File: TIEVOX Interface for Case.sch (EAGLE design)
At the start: 22 parts, among them U4 CAT24C32.UDFN8

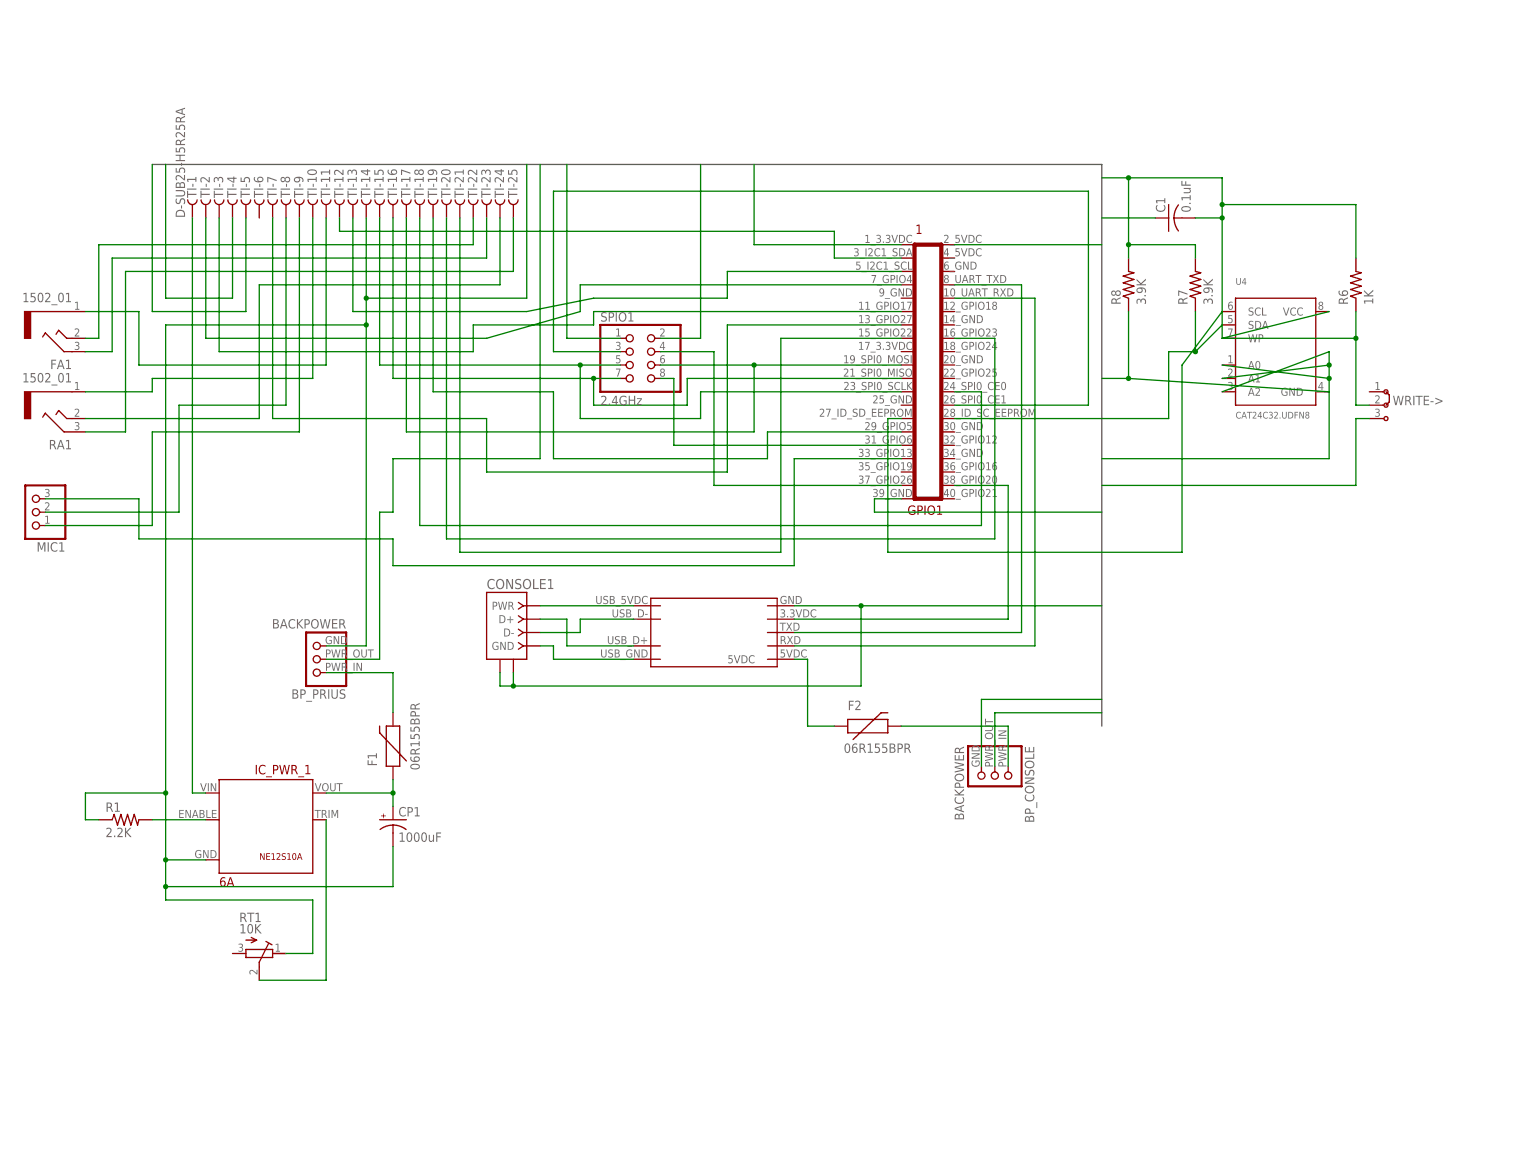
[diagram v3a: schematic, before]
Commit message: Updated TIEVOX Interface for Case:
- Removed console circuit
- Replaced audio jacks to use ones purchased
- Remapped circuit schematic
- Added backpower protection back in
- Still needs traces drawn.
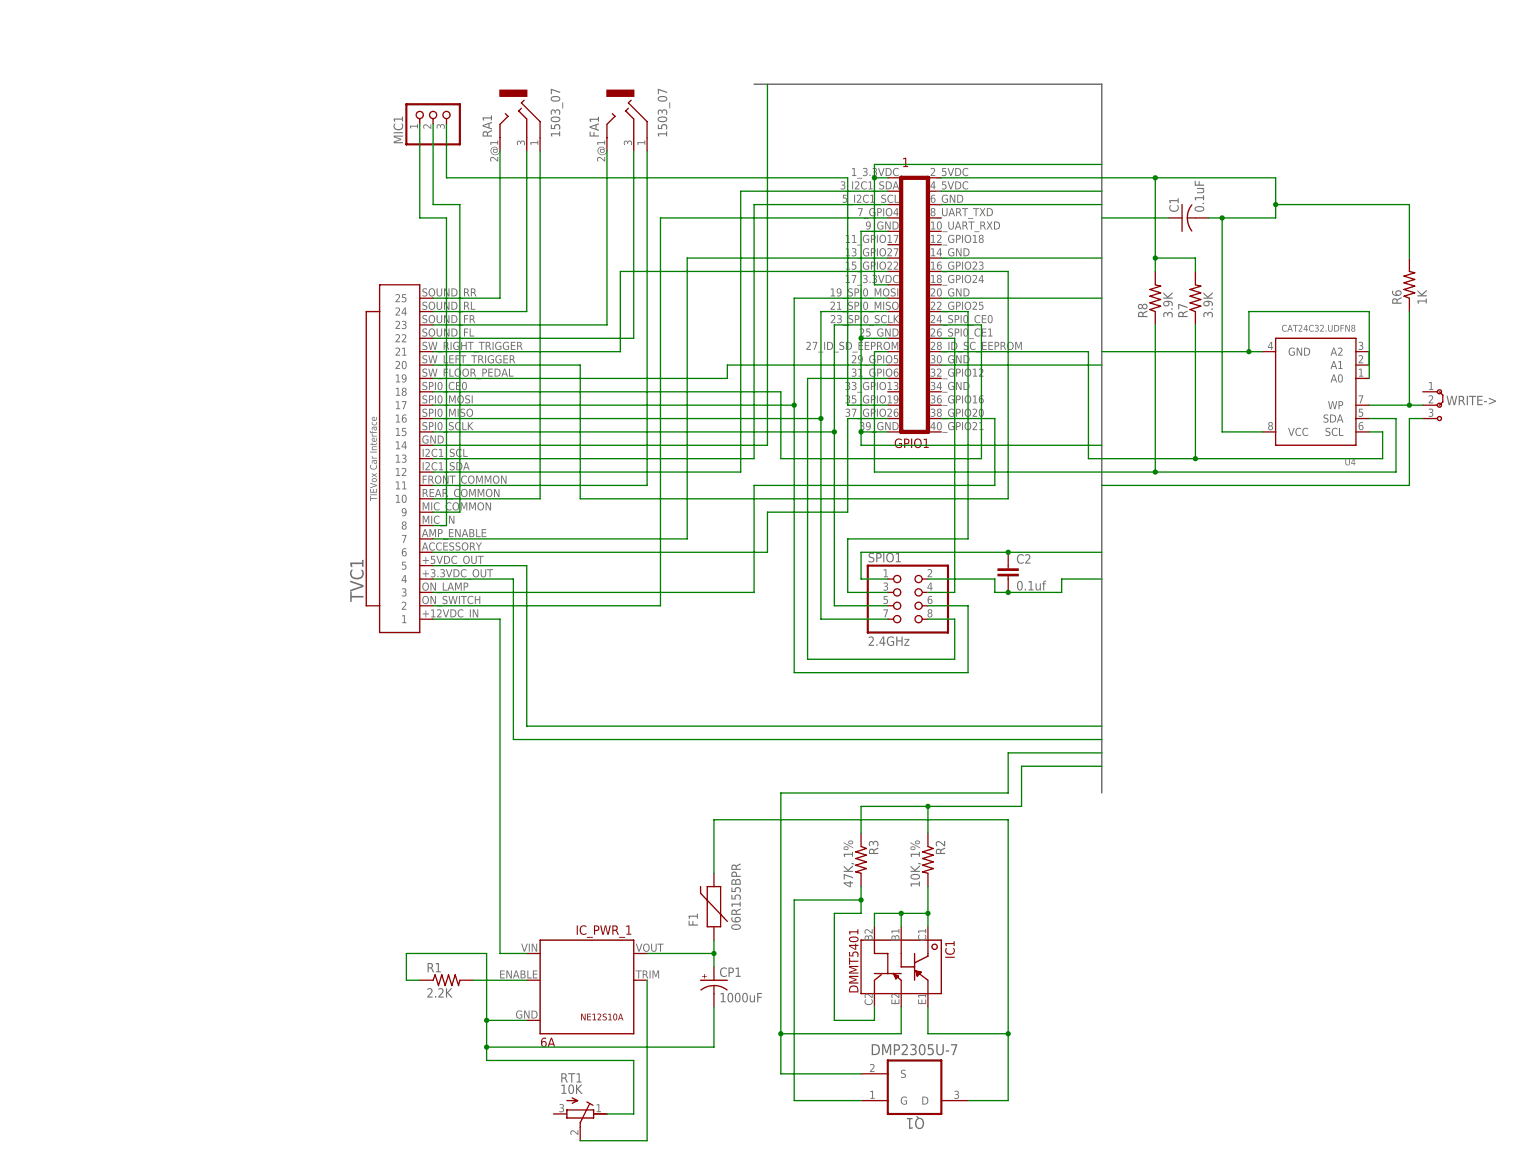
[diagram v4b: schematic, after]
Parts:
- removed BP_CONSOLE, BP_PRIUS: BACKPOWER, connectors:BACKPOWER
- removed CONSOLE1: (no value), connector:USB-RA
- removed F2: 06R155BPR, SparkFun-PowerIC:PTCPTH
- removed TI: D-SUB25-H5R25RA, con-thomas-betts:D-SUB25-H5R25RA
- removed UART1: GS27159, packages:GS27159
- added C2: 0.1uf, capacitor-wima:C5/2.5
- added IC1: DMMT5401, Diodes_Inc_By_element14_Batch_1:DMMT5401DMMT
- added Q1: DMP2305U-7, Diodes_Inc_By_element14_Batch_1:DMP2305U-7
- added R2: 10K, 1%, adafruit:R-US_0207/7
- added R3: 47K, 1%, adafruit:R-US_0207/7
- added TVC1: TIEVox Car Interface, connectors:TIEVOX_CAR_25
- FA1, RA1: value 1502_01 -> 1503_07; device con-lumberg:1502_01 -> con-lumberg:1503_07
- GPIO1: value RPI_GPIO_FEMALE_LOWER -> RPI_GPIO_MALE_SHROUD; device connectors:RPI_GPIO_FEMALE_LOWER -> connectors:RPI_GPIO_MALE_SHROUD
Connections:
- removed net 5VDC: F2.1, UART1.5VDC
- removed net CONSOLE_ON: GPIO1.38_GPIO20, UART1.3.3VDC
- removed net N$11 (its old number): GPIO1.29_GPIO5, TI-19.F
- removed net N$31: BP_CONSOLE.PWR_IN, F2.2
- removed net N$36: MIC1.1, TI-9.F
- removed net N$37: MIC1.2, TI-8.F
- removed net N$38: GPIO1.27_ID_SC_EEPROM, U4.SCL
- removed net N$40: GPIO1.28_ID_SC_EEPROM, R7.1, U4.SDA
- removed net N$41: GPIO1.33_GPIO13, MIC1.3
- new net IN: F1.2, IC1.E1, Q1.D
- new net N$32: IC1.B1, IC1.B2, IC1.C1, R2.2
- new net N$33: IC1.C2, Q1.G, R3.2
- new net N$5: FA1.1, TVC1.11
- net +3.3VDC: now also C2.2, GPIO1.17_3.3VDC, TVC1.4; no longer TI-4.F
- net +5VDC: now also GPIO1.4_5VDC, IC1.E2, Q1.S, TVC1.5; no longer BP_CONSOLE.PWR_OUT, BP_PRIUS.PWR_OUT, TI-5.F
- net GND: now also C2.1, GPIO1.14_GND, GPIO1.20_GND, GPIO1.25_GND, GPIO1.30_GND, GPIO1.6_GND, GPIO1.9_GND, R2.1, R3.1, TVC1.14; no longer BP_CONSOLE.GND, BP_PRIUS.GND, CONSOLE1.SHIELD1, CONSOLE1.SHIELD2, R8.1, TI-14.F, U4.A1, U4.A2, UART1.GND
- net N$1: now also U4.A1, U4.A2; no longer GPIO1.19_SPI0_MOSI, SPIO1.6, TI-17.F
- net N$10: now also GPIO1.19_SPI0_MOSI, SPIO1.6, TVC1.17; no longer GPIO1.24_SPI0_CE0, TI-18.F
- net N$12: now also RA1.2, TVC1.25; no longer GPIO1.16_GPIO23, TI-20.F
- net N$13: now also RA1.3, TVC1.24; no longer GPIO1.15_GPIO22, TI-21.F
- net N$14: now also FA1.2, TVC1.23; no longer CONSOLE1.GND, UART1.USB_GND
- net N$15: now also FA1.3, TVC1.22; no longer CONSOLE1.PWR, UART1.USB_5VDC
- net N$16: now also MIC1.1, TVC1.8; no longer CONSOLE1.D-, UART1.USB_D-
- net N$17: now also MIC1.2, TVC1.9; no longer CONSOLE1.D+, UART1.USB_D+
- net N$18: now also GPIO1.5_I2C1_SCL, TVC1.13; no longer GPIO1.8_UART0_TXD, UART1.TXD
- net N$19: now also GPIO1.3_I2C1_SDA, TVC1.12; no longer GPIO1.10_UART0_RXD, UART1.RXD
- net N$2: now also GPIO1.28_ID_SC_EEPROM, R7.1, U4.SCL; no longer GPIO1.21_SPI0_MISO, SPIO1.7, TI-16.F
- net N$20: now also GPIO1.24_SPI0_CE0, TVC1.18; no longer FA1.1, TI-11.F
- net N$21: now also GPIO1.37_GPIO26, TVC1.6; no longer RA1.1, TI-10.F
- net N$22: now also GPIO1.35_GPIO19, MIC1.3; no longer RA1.3, TI-24.F
- net N$23: now also GPIO1.13_GPIO27, TVC1.7; no longer RA1.2, TI-25.F
- net N$24: now also GPIO1.7_GPIO4, TVC1.2; no longer FA1.2, TI-23.F
- net N$25: now also GPIO1.38_GPIO20, TVC1.3; no longer FA1.3, TI-22.F
- net N$26: now also GPIO1.29_GPIO5, TVC1.19; no longer GPIO1.3_I2C1_SDA, TI-12.F
- net N$27: now also GPIO1.15_GPIO22, TVC1.21; no longer GPIO1.5_I2C1_SCL, TI-13.F
- net N$3: now also GPIO1.27_ID_SC_EEPROM, R8.1, U4.SDA; no longer GPIO1.23_SPI0_SCLK, SPIO1.5, TI-15.F
- net N$30: now also GPIO1.16_GPIO23, TVC1.20; no longer BP_PRIUS.PWR_IN, F1.2
- net N$4: now also GPIO1.22_GPIO25; no longer GPIO1.26_SPI0_CE1
- net N$6: now also RA1.1, TVC1.10; no longer GPIO1.37_GPIO26, SPIO1.4
- net N$7: now also GPIO1.26_SPI0_CE1, SPIO1.4; no longer GPIO1.7_GPIO4, TI-2.F
- net N$8: now also GPIO1.23_SPI0_SCLK, SPIO1.5, TVC1.15; no longer GPIO1.11_GPIO17, TI-3.F
- net N$9: now also GPIO1.21_SPI0_MISO, SPIO1.7, TVC1.16; no longer GPIO1.13_GPIO27, TI-7.F
- net PWR12_IN: now also TVC1.1; no longer TI-1.F
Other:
- note added: "Audio Connections"
- note added: "Car Interface"
- note added: "Car Power Conversion"
- note added: "GPIO"
- note added: "HAT EEPROM"
- note added: "SPI 2.4GHz nRF24L01P-MODULE-PCB"
- moved on the sheet: C1, CP1, F1, GPIO1, IC_PWR_1, MIC1, R1, R6, R7, R8, RT1, SPIO1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

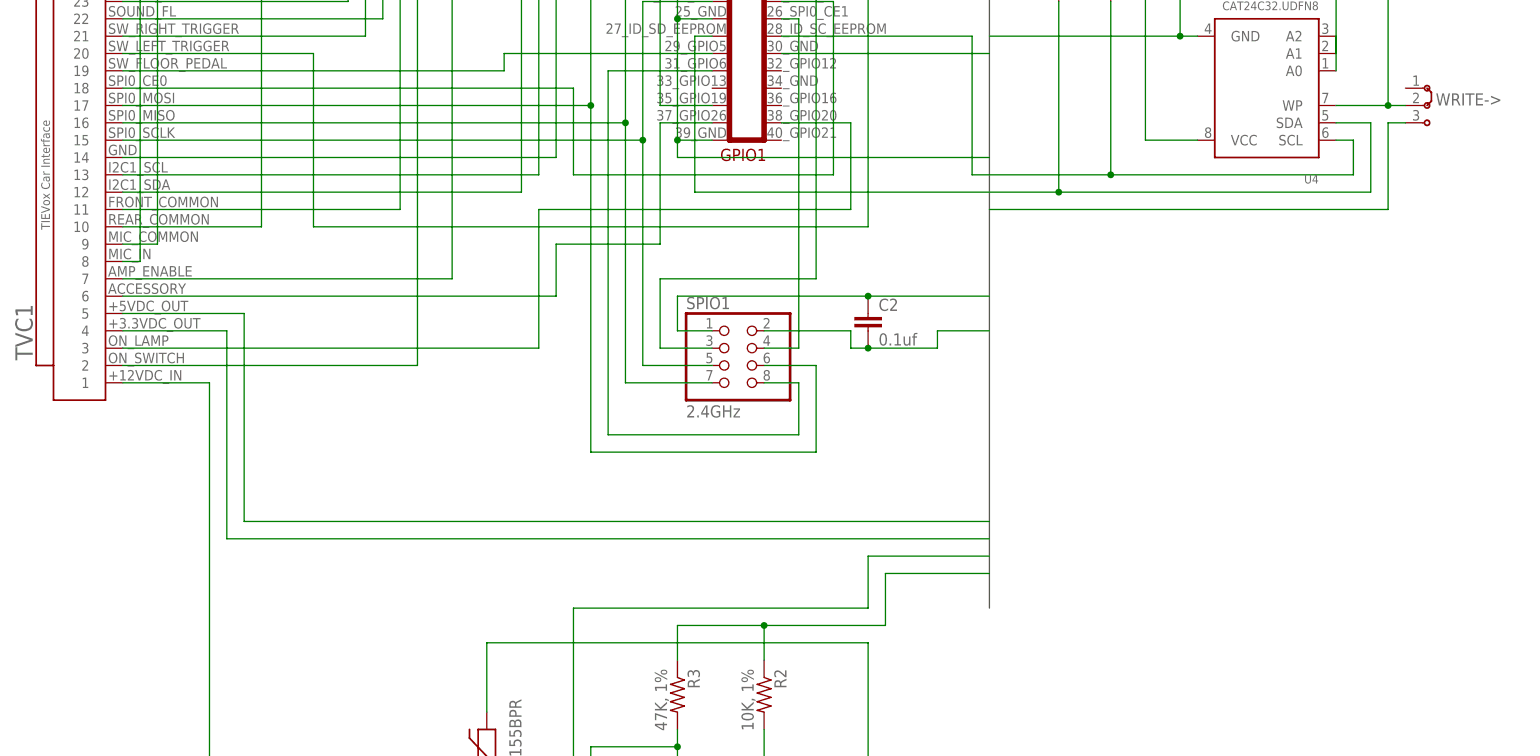
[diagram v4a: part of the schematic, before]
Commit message: Added printables for split/protect circuit for fab of board.
Added Accessory Relay header to interface board.
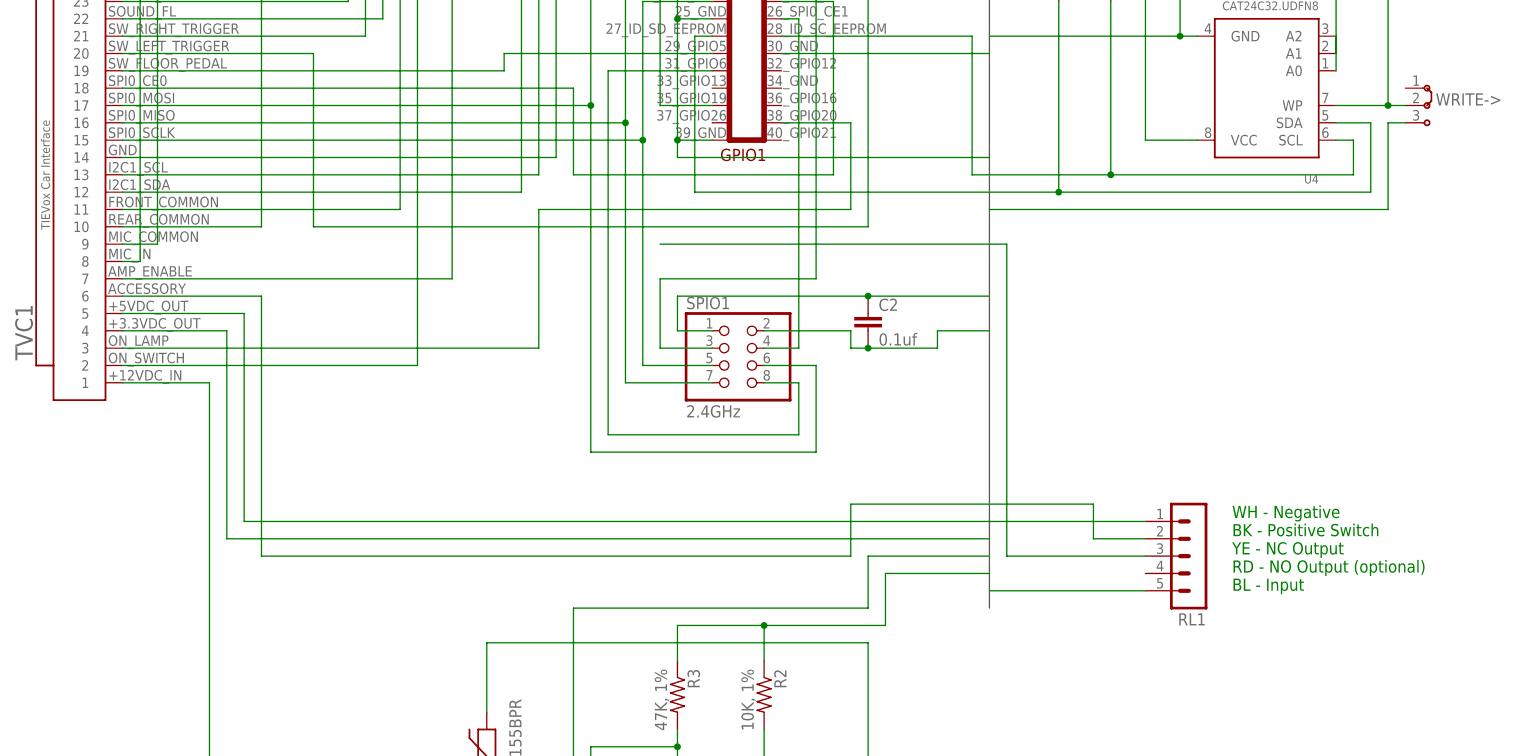
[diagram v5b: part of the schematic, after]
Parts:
- added RL1: (no value), con-lstb:MA05-1
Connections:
- new net N$31: RL1.3
- net +3.3VDC: now also RL1.5
- net GND: now also RL1.1
- net N$21: now also RL1.2; no longer GPIO1.37_GPIO26
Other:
- note added: "Accessory Signal Relay Header"
- note added: "WH - Negative BK - Positive Switch YE - NC Output RD - NO Output (optional) BL - Input"
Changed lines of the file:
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@@
 <part name="TVC1" library="connectors" deviceset="TIEVOX_CAR_25" device="" value="TIEVox Car Interface"/>
 <part name="C2" library="capacitor-wima" deviceset="C" device="5/2.5" value="0.1uf"/>
+<part name="RL1" library="con-lstb" deviceset="MA05-1" device=""/>
 </parts>
 <sheets>
@@
 <wire x1="27.94" y1="-91.44" x2="162.56" y2="-91.44" width="0.1524" layer="90"/>
 <wire x1="162.56" y1="-91.44" x2="162.56" y2="-20.32" width="0.1524" layer="90"/>
-<wire x1="162.56" y1="-20.32" x2="27.94" y2="-20.32" width="0.1524" layer="90"/>
-<wire x1="27.94" y1="-20.32" x2="27.94" y2="-91.44" width="0.1524" layer="90"/>
+<wire x1="162.56" y1="-20.32" x2="28.194" y2="-21.082" width="0.1524" layer="90"/>
+<wire x1="28.194" y1="-21.082" x2="27.94" y2="-91.44" width="0.1524" layer="90"/>
 <wire x1="27.94" y1="96.52" x2="91.44" y2="96.52" width="0.1524" layer="90"/>
 <wire x1="91.44" y1="96.52" x2="91.44" y2="114.3" width="0.1524" layer="90"/>
@@
 <wire x1="160.02" y1="27.94" x2="104.14" y2="27.94" width="0.1524" layer="90"/>
 <wire x1="104.14" y1="27.94" x2="104.14" y2="-2.54" width="0.1524" layer="90"/>
+<text x="198.12" y="2.54" size="1.778" layer="90" align="center">Accessory Signal
+Relay Header</text>
+<text x="200.66" y="-20.32" size="1.778" layer="91">WH - Negative
+BK - Positive Switch
+YE - NC Output
+RD - NO Output (optional)
+BL - Input</text>
 </plain>
 <instances>
@@
 <instance part="TVC1" gate="DSUB25" x="35.56" y="40.64" rot="R90"/>
 <instance part="C2" gate="G$1" x="147.32" y="20.32"/>
+<instance part="RL1" gate="G$1" x="195.58" y="-15.24" rot="R180"/>
 </instances>
 <busses>
@@
 <wire x1="38.1" y1="43.18" x2="101.6" y2="43.18" width="0.1524" layer="91"/>
 <wire x1="101.6" y1="43.18" x2="101.6" y2="111.76" width="0.1524" layer="91"/>
+</segment>
+<segment>
+<pinref part="RL1" gate="G$1" pin="1"/>
+<wire x1="187.96" y1="-10.16" x2="165.1" y2="-10.16" width="0.1524" layer="91"/>
 </segment>
 </net>
@@
 <wire x1="53.34" y1="17.78" x2="38.1" y2="17.78" width="0.1524" layer="91"/>
 </segment>
+<segment>
+<pinref part="RL1" gate="G$1" pin="5"/>
+<wire x1="187.96" y1="-20.32" x2="165.1" y2="-20.32" width="0.1524" layer="91"/>
+</segment>
 </net>
 <net name="PWR12_TRIM" class="0">
@@
 </segment>
 </net>
-<net name="N$21" class="0">
-<segment>
-<pinref part="TVC1" gate="DSUB25" pin="6"/>
-<wire x1="38.1" y1="22.86" x2="101.6" y2="22.86" width="0.1524" layer="91"/>
-<wire x1="101.6" y1="22.86" x2="101.6" y2="30.48" width="0.1524" layer="91"/>
-<wire x1="101.6" y1="30.48" x2="116.84" y2="30.48" width="0.1524" layer="91"/>
-<wire x1="116.84" y1="30.48" x2="116.84" y2="48.26" width="0.1524" layer="91"/>
-<pinref part="GPIO1" gate="G$1" pin="37_GPIO26"/>
-<wire x1="116.84" y1="48.26" x2="124.46" y2="48.26" width="0.1524" layer="91"/>
-</segment>
-</net>
 <net name="N$22" class="0">
 <segment>
@@
 </segment>
 </net>
+<net name="N$21" class="0">
+<segment>
+<pinref part="TVC1" gate="DSUB25" pin="6"/>
+<wire x1="38.1" y1="22.86" x2="58.42" y2="22.86" width="0.1524" layer="91"/>
+<wire x1="58.42" y1="22.86" x2="58.42" y2="-15.24" width="0.1524" layer="91"/>
+<wire x1="58.42" y1="-15.24" x2="144.78" y2="-15.24" width="0.1524" layer="91"/>
+<wire x1="144.78" y1="-15.24" x2="144.78" y2="-7.62" width="0.1524" layer="91"/>
+<wire x1="144.78" y1="-7.62" x2="180.34" y2="-7.62" width="0.1524" layer="91"/>
+<wire x1="180.34" y1="-7.62" x2="180.34" y2="-12.7" width="0.1524" layer="91"/>
+<pinref part="RL1" gate="G$1" pin="2"/>
+<wire x1="180.34" y1="-12.7" x2="187.96" y2="-12.7" width="0.1524" layer="91"/>
+</segment>
+</net>
+<net name="N$31" class="0">
+<segment>
+<pinref part="RL1" gate="G$1" pin="3"/>
+<wire x1="187.96" y1="-15.24" x2="167.64" y2="-15.24" width="0.1524" layer="91"/>
+<wire x1="167.64" y1="-15.24" x2="167.64" y2="30.48" width="0.1524" layer="91"/>
+<wire x1="167.64" y1="30.48" x2="116.84" y2="30.48" width="0.1524" layer="91"/>
+</segment>
+</net>
